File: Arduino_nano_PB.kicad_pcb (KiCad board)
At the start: 2 copper layers, 100 x 40 mm, 44 parts, among them CON1 BARREL_JACK, P1 CONN_01X02, P7 CONN_01X04, Q1 BC547, Q2 BC547, Q3 BC547, Q4 Q_NPN_EBC, Q5 Q_NPN_EBC, Q6 Q_NPN_EBC, Q7 Q_NPN_EBC, Q8 Q_NPN_EBC, U1 LM7805CT, U2 74HC595, U3 Matriz_5x7_Anodo_Filas, U4 Arduino_Nano

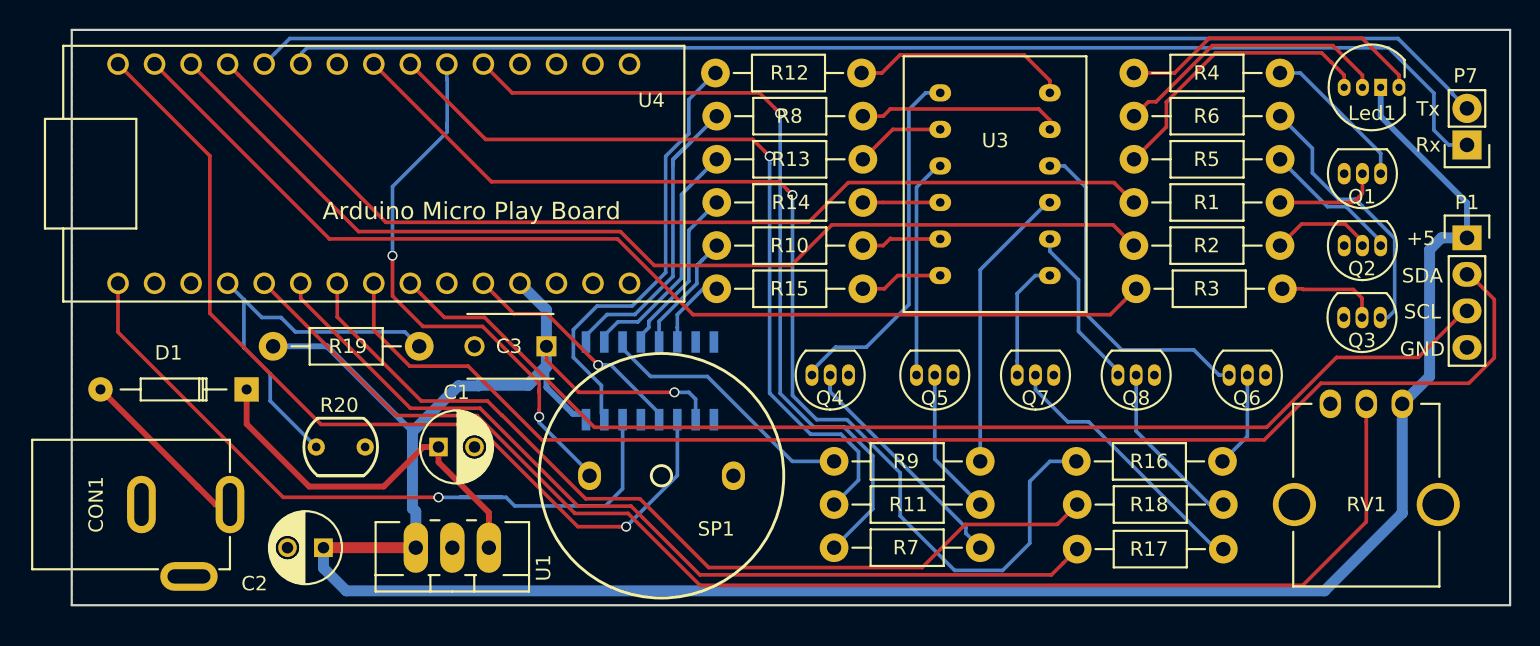
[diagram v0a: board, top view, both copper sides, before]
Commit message: añadir valores en esquema y reordenar PCB
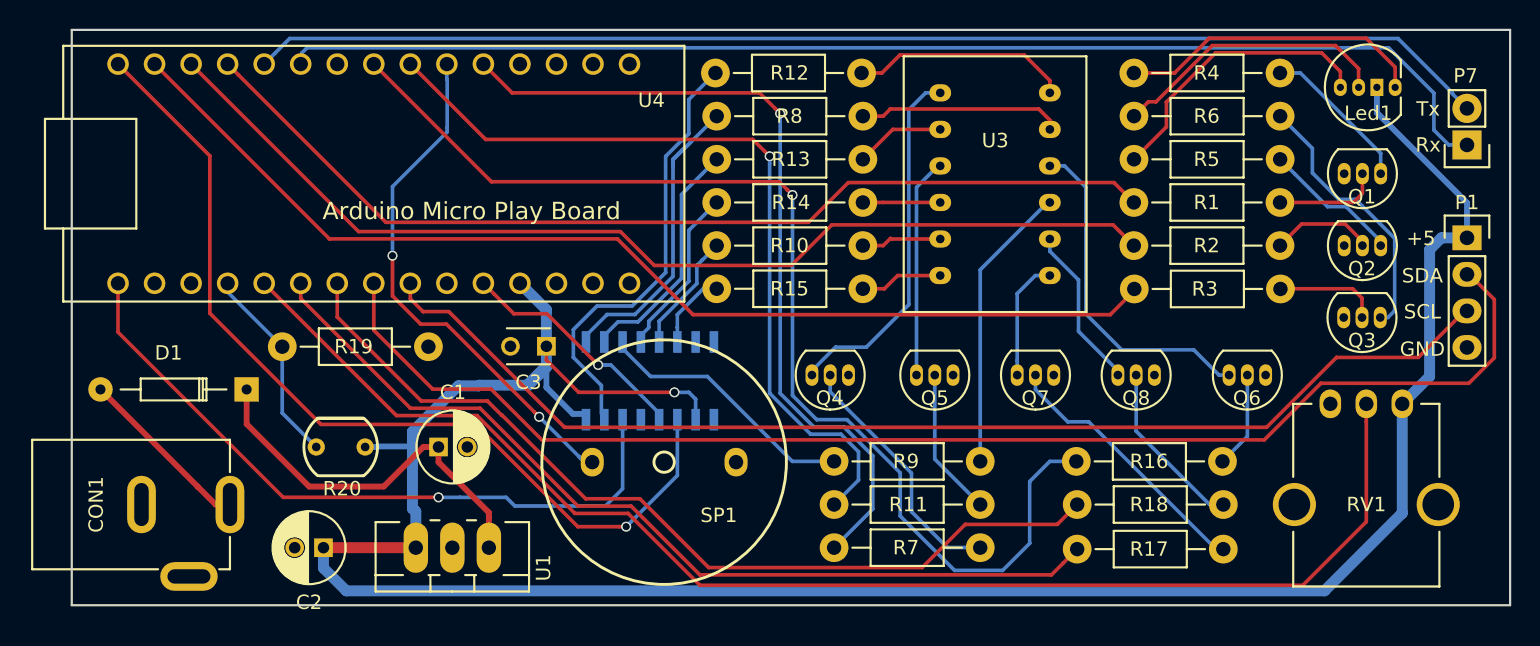
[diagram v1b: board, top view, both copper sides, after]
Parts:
- C1, C2: footprint Capacitors_ThroughHole:C_Radial_D5_L11_P2.5 -> Capacitors_ThroughHole:C_Radial_D5_L11_P2
- C3: value C -> 100n; footprint Capacitors_ThroughHole:C_Disc_D6_P5 -> Capacitors_ThroughHole:C_Disc_D3_P2.5
- D1: value D -> 1N4002
- Led1: value Led_RGB_Anodo_Comun -> Led_RGB
- Q4, Q5, Q6, Q7, Q8: value Q_NPN_EBC -> 2N3904BU
- R1, R2, R3: value R -> 4K7
- R10, R12, R13, R14, R15, R8, R9: value R -> 120
- R11, R16, R17, R18, R19, R7: value R -> 1K
- R20: value Photores -> LDR
- R4, R5, R6: value R -> 100
- RV1: value POT -> 10K
- SP1: value SPEAKER -> BUZZER
- U3: value Matriz_5x7_Anodo_Filas -> Matriz_5x7
- moved R19 10.8 mm to (134.8, 62.0), turned to 180 degrees
- moved SP1 0.96 mm to (151.2, 70.1)
- moved Led1 0.26 mm to (200.1, 44.0)
- moved R3 0.13 mm to (194.0, 58.0)
- turned R20 to 180 degrees
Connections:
- R19 pad 1: +5V -> GND
- R20 pad 1: /A0 -> +5V
- R20 pad 2: GND -> /A0
- U2 pad 7: (no net) -> Net-(U2-Pad7)
- U2 pad 9: (no net) -> Net-(U2-Pad9)
- U4 pad 1: (no net) -> Net-(U4-Pad1)
- U4 pad 17: (no net) -> +3V3
- U4 pad 18: (no net) -> Net-(U4-Pad18)
- U4 pad 2: (no net) -> Net-(U4-Pad2)
- U4 pad 25: (no net) -> Net-(U4-Pad25)
- U4 pad 28: (no net) -> Net-(U4-Pad28)
- U4 pad 3: (no net) -> Net-(U4-Pad3)
- U4 pad 30: (no net) -> Net-(U4-Pad30)
- U4 pad 9: (no net) -> Net-(U4-Pad9)
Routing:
- net /A0: track 27.6 -> 14.1 mm
- net +5V: track 190.5 -> 181.8 mm
- net /D13: track 51.7 -> 48.8 mm
- net /D3: track 38.8 -> 36.8 mm
- net Net-(Q4-Pad2): track 16.5 -> 17.7 mm
- net /A5: track 81.0 -> 81.6 mm

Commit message: Añadir serigrafia capa bottom
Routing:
- net Net-(C1-Pad1): track 27.1 -> 26.2 mm
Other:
- board text added: "Bu-D11"
- board text added: "Buzz-D3"
- board text added: "ClkIn-D12"
- board text added: "ClkOut-A7"
- board text added: "Col1-D2"
- board text added: "Col2-D4"
- board text added: "Col3-D5"
- board text added: "Col4-A2"
- board text added: "Col5-A3"
- board text added: "Din-D13"
- board text added: "Gn-D10"
- board text added: "LDR-A0"
- board text added: "Pot-A1"
- board text added: "Rd-D9"
- board text added: "Rx-D7"
- board text added: "SERIAL"
- board text added: "Tx-D8"
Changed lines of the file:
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@@
     (links 85)
     (no_connects 0)
-    (area 109.924999 39.924999 210.075001 80.075001)
+    (area 106.868999 39.924999 211.8998 80.075001)
     (thickness 1.6)
-    (drawings 11)
-    (tracks 399)
+    (drawings 28)
+    (tracks 398)
     (zones 0)
     (modules 44)
@@
     (47 F.CrtYd user)
     (48 B.Fab user)
-    (49 F.Fab user)
+    (49 F.Fab user hide)
   )
   (setup
@@
       (linewidth 0.100000)
       (plotframeref false)
-      (viasonmask true)
+      (viasonmask false)
       (mode 1)
       (useauxorigin false)
@@
   (module Sensores:LDR_TOKEN_PGM5_Series (layer F.Cu)
     (at 128.7 69 180)
-    (fp_text reference R20 (at -0.1 -2.9 180) (layer F.SilkS)
+    (fp_text reference R20 (at -0.0018 -2.9836 180) (layer F.SilkS)
       (effects (font (size 1 1) (thickness 0.15)))
     )
@@
     (descr "Radial Electrolytic Capacitor 5mm x Length 11mm, Pitch 2mm")
     (tags "Electrolytic Capacitor")
-    (fp_text reference C2 (at 1 -3.8 180) (layer F.SilkS)
+    (fp_text reference C2 (at 4.5386 -2.2574 180) (layer F.SilkS)
       (effects (font (size 1 1) (thickness 0.15)))
     )
@@
     )
   )
+  (gr_text ClkOut-A7 (at 156.0068 76.4794) (layer B.SilkS)
+    (effects (font (size 1 1) (thickness 0.2)) (justify mirror))
+  )
+  (gr_text ClkIn-D12 (at 156.0576 74.5998) (layer B.SilkS)
+    (effects (font (size 1 1) (thickness 0.2)) (justify mirror))
+  )
+  (gr_text Din-D13 (at 156.718 72.7964) (layer B.SilkS)
+    (effects (font (size 1 1) (thickness 0.2)) (justify mirror))
+  )
+  (gr_text Buzz-D3 (at 144.9324 72.9488) (layer B.SilkS)
+    (effects (font (size 1 1) (thickness 0.2)) (justify mirror))
+  )
+  (gr_text Bu-D11 (at 189.1284 48.9712) (layer B.SilkS)
+    (effects (font (size 1 1) (thickness 0.2)) (justify mirror))
+  )
+  (gr_text Gn-D10 (at 189.1538 45.974) (layer B.SilkS)
+    (effects (font (size 1 1) (thickness 0.2)) (justify mirror))
+  )
+  (gr_text Rd-D9 (at 189.1538 42.9768) (layer B.SilkS)
+    (effects (font (size 1 1) (thickness 0.2)) (justify mirror))
+  )
+  (gr_text LDR-A0 (at 128.8796 66.04) (layer B.SilkS)
+    (effects (font (size 1 1) (thickness 0.2)) (justify mirror))
+  )
+  (gr_text Pot-A1 (at 199.9996 69.9262) (layer B.SilkS)
+    (effects (font (size 1 1) (thickness 0.2)) (justify mirror))
+  )
+  (gr_text Col5-A3 (at 165.481 64.0334 90) (layer B.SilkS)
+    (effects (font (size 1 1) (thickness 0.2)) (justify mirror))
+  )
+  (gr_text Col4-A2 (at 172.7454 64.0334 90) (layer B.SilkS)
+    (effects (font (size 1 1) (thickness 0.2)) (justify mirror))
+  )
+  (gr_text Col3-D5 (at 179.7558 64.0334 90) (layer B.SilkS)
+    (effects (font (size 1 1) (thickness 0.2)) (justify mirror))
+  )
+  (gr_text Col2-D4 (at 186.7662 64.0334 90) (layer B.SilkS)
+    (effects (font (size 1 1) (thickness 0.2)) (justify mirror))
+  )
+  (gr_text Col1-D2 (at 194.4878 64.0334 90) (layer B.SilkS)
+    (effects (font (size 1 1) (thickness 0.2)) (justify mirror))
+  )
+  (gr_text Rx-D7 (at 203.1746 47.9552) (layer B.SilkS)
+    (effects (font (size 1 1) (thickness 0.2)) (justify mirror))
+  )
+  (gr_text Tx-D8 (at 203.1746 45.72) (layer B.SilkS)
+    (effects (font (size 1 1) (thickness 0.2)) (justify mirror))
+  )
+  (gr_text SERIAL (at 206.2734 42.799) (layer B.SilkS)
+    (effects (font (size 1 1) (thickness 0.2)) (justify mirror))
+  )
   (gr_text "Arduino Micro Play Board" (at 137.8 52.6) (layer F.SilkS)
     (effects (font (size 1.2 1.2) (thickness 0.2)))
@@
   (gr_line (start 110 40) (end 110 80) (layer Edge.Cuts) (width 0.15))
   (gr_line (start 110 40) (end 210 40) (layer Edge.Cuts) (width 0.15))
+  (segment (start 143 62) (end 143 63.462) (width 0.762) (layer B.Cu) (net 2))
+  (segment (start 143 63.462) (end 141.717223 64.744777) (width 0.762) (layer B.Cu) (net 2))
+  (segment (start 141.717223 64.744777) (end 138.305223 64.744777) (width 0.762) (layer B.Cu) (net 2))
+  (segment (start 138.305223 64.744777) (end 138.3 64.75) (width 0.762) (layer B.Cu) (net 2))
   (segment (start 200.7362 44) (end 200.7362 45.756611) (width 0.4064) (layer B.Cu) (net 2))
   (segment (start 200.7362 45.756611) (end 207 52.020411) (width 0.4064) (layer B.Cu) (net 2))
@@
   (segment (start 145.246 65.2) (end 151.9 65.2) (width 0.254) (layer F.Cu) (net 2))
   (via (at 151.9 65.2) (size 0.7) (drill 0.5) (layers F.Cu B.Cu) (net 2))
-  (segment (start 141.7556 64.7064) (end 138.3436 64.7064) (width 0.762) (layer B.Cu) (net 2))
-  (segment (start 138.3436 64.7064) (end 138.3 64.75) (width 0.762) (layer B.Cu) (net 2))
-  (segment (start 143 62) (end 143 63.462) (width 0.762) (layer B.Cu) (net 2) (status 10))
-  (segment (start 143 63.462) (end 141.7556 64.7064) (width 0.762) (layer B.Cu) (net 2))
   (segment (start 141.3564 64.75) (end 138.3 64.75) (width 0.4064) (layer B.Cu) (net 2))
   (segment (start 133.687638 67.939064) (end 136.876702 64.75) (width 0.762) (layer B.Cu) (net 2))
@@
   (segment (start 127 69) (end 124.6378 66.6378) (width 0.254) (layer B.Cu) (net 6))
   (segment (start 124.6378 66.6378) (end 124.6378 62.0268) (width 0.254) (layer B.Cu) (net 6))
-  (segment (start 135.5 69) (end 134.4436 69) (width 0.4064) (layer F.Cu) (net 7))
-  (segment (start 134.4436 69) (end 131.6936 71.75) (width 0.4064) (layer F.Cu) (net 7))
-  (segment (start 131.6936 71.75) (end 126.50922 71.75) (width 0.4064) (layer F.Cu) (net 7))
-  (segment (start 126.50922 71.75) (end 122.16 67.40078) (width 0.4064) (layer F.Cu) (net 7))
-  (segment (start 122.16 67.40078) (end 122.16 65) (width 0.4064) (layer F.Cu) (net 7))
-  (segment (start 135.5 69) (end 135.5 70.0564) (width 0.4064) (layer F.Cu) (net 7))
-  (segment (start 135.5 70.0564) (end 139 73.5564) (width 0.4064) (layer F.Cu) (net 7))
-  (segment (start 139 73.5564) (end 139 73.84354) (width 0.4064) (layer F.Cu) (net 7))
-  (segment (start 139 73.84354) (end 139 76) (width 0.4064) (layer F.Cu) (net 7) (status 20))
+  (segment (start 135.5 69) (end 135.5 70.412) (width 0.762) (layer F.Cu) (net 7))
+  (segment (start 139 73.912) (end 139 76) (width 0.762) (layer F.Cu) (net 7))
+  (segment (start 135.5 70.412) (end 139 73.912) (width 0.762) (layer F.Cu) (net 7))
+  (segment (start 122.16 65) (end 122.16 67.2198) (width 0.762) (layer F.Cu) (net 7))
+  (segment (start 122.16 67.2198) (end 125.6538 70.7136) (width 0.762) (layer F.Cu) (net 7))
+  (segment (start 125.6538 70.7136) (end 132.2832 70.7136) (width 0.762) (layer F.Cu) (net 7))
+  (segment (start 132.2832 70.7136) (end 133.9968 69) (width 0.762) (layer F.Cu) (net 7))
+  (segment (start 133.9968 69) (end 135.5 69) (width 0.762) (layer F.Cu) (net 7))
   (segment (start 159.251868 65.276109) (end 159.251868 46.313275) (width 0.254) (layer B.Cu) (net 8))
   (segment (start 163 76) (end 165.689574 73.310426) (width 0.254) (layer B.Cu) (net 8) (status 10))
@@
   (segment (start 123.38 57.62) (end 132.576022 66.816022) (width 0.254) (layer F.Cu) (net 40) (status 10))
   (segment (start 138.17915 66.816022) (end 144.97915 73.616022) (width 0.254) (layer F.Cu) (net 40))
-  (segment (start 121 73) (end 120 73) (width 0.4064) (layer F.Cu) (net 41) (status 30))
-  (segment (start 118.75 71.75) (end 112 65) (width 0.4064) (layer F.Cu) (net 41) (status 20))
-  (segment (start 120 73) (end 118.75 71.75) (width 0.4064) (layer F.Cu) (net 41) (status 10))
+  (segment (start 121 73) (end 120 73) (width 0.762) (layer F.Cu) (net 41) (status 30))
+  (segment (start 118.75 71.75) (end 112 65) (width 0.762) (layer F.Cu) (net 41) (status 20))
+  (segment (start 120 73) (end 118.75 71.75) (width 0.762) (layer F.Cu) (net 41) (status 10))
   (segment (start 142.497241 66.902759) (end 145.266682 69.6722) (width 0.254) (layer B.Cu) (net 42))
   (segment (start 145.266682 69.6722) (end 145.5496 69.955118) (width 0.254) (layer B.Cu) (net 42))

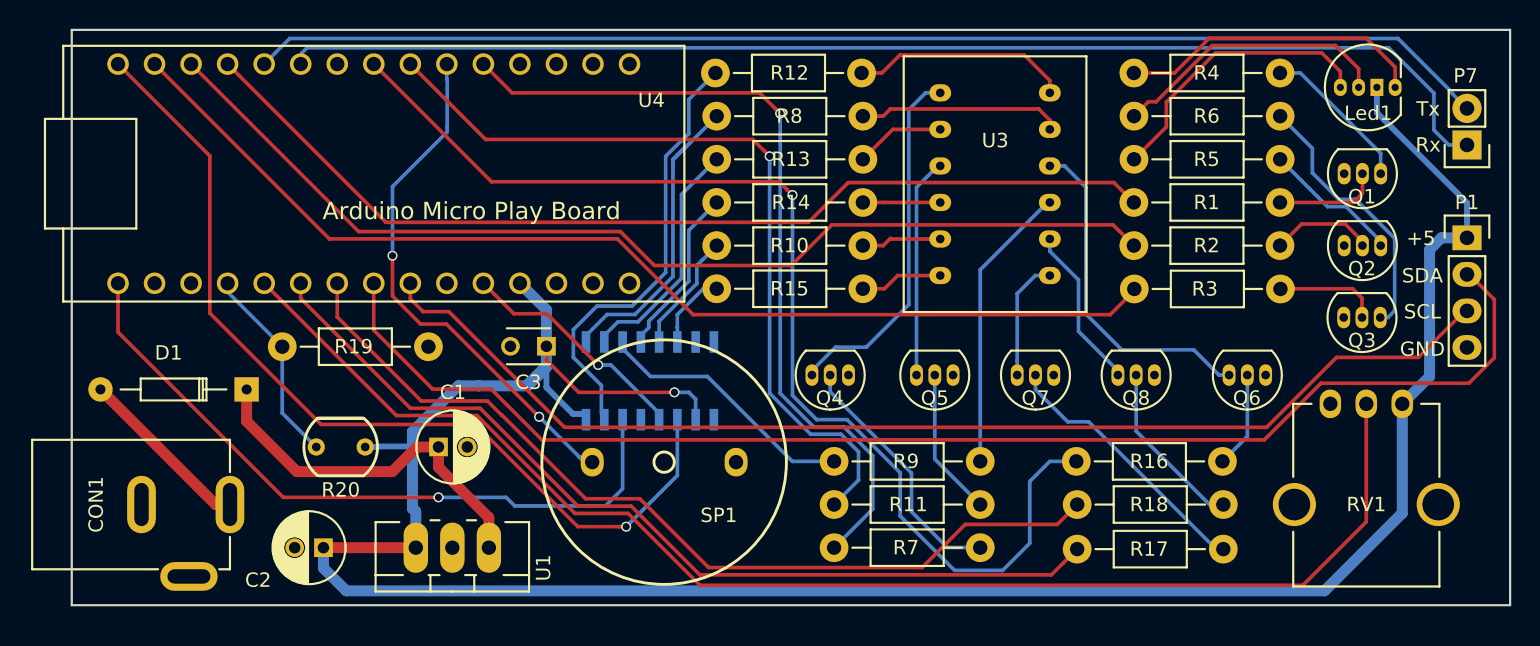
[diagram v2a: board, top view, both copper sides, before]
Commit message: corregir errata en readme y capa de serigrafia superior
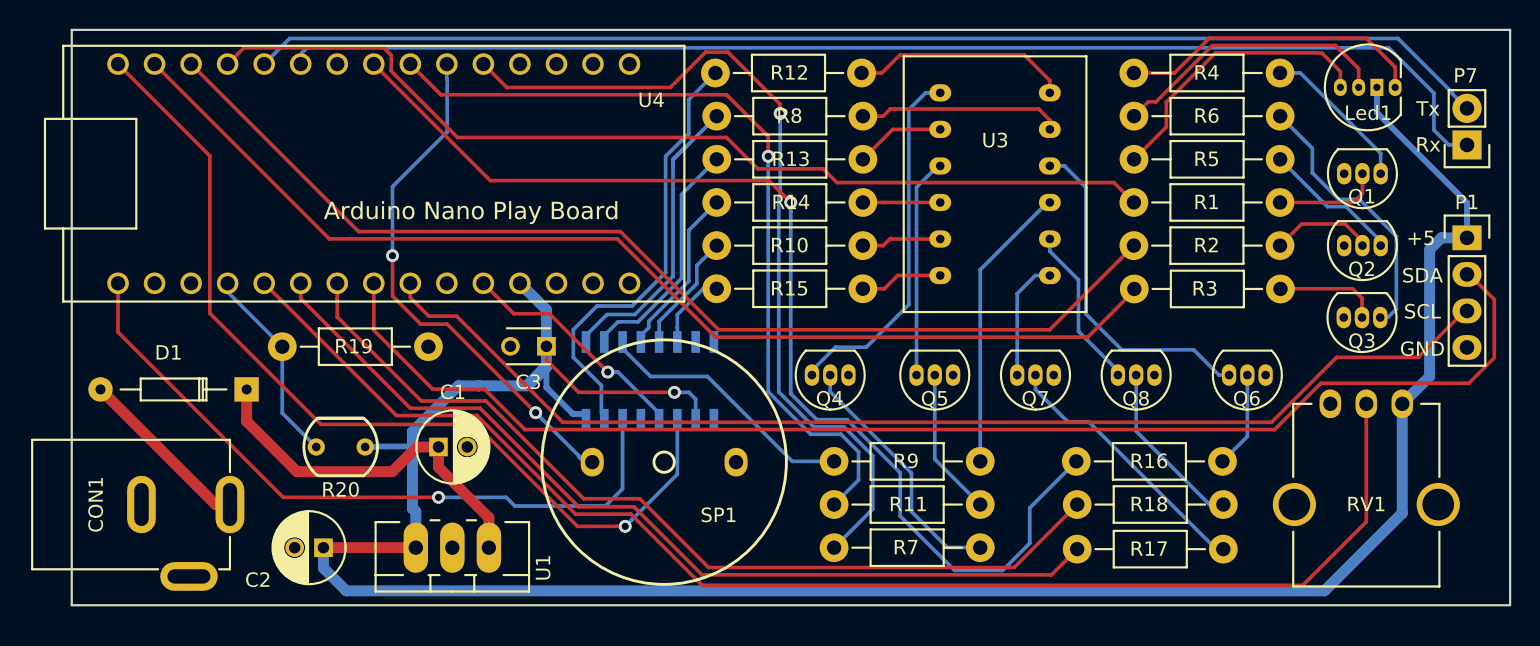
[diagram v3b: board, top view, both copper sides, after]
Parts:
- Q1, Q2, Q3, Q4, Q5, Q6, Q7, Q8: footprint TO_SOT_Packages_THT:TO-92_Inline_Narrow_Oval -> Transistors:TO-92_EnLinea_Estrecho_Oval
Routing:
- net /D10: track 73.1 -> 75.6 mm
- net /D2: track 57.3 -> 59.7 mm
- net /D5: track 79.0 -> 77.5 mm
- net /D11: track 76.2 -> 77.5 mm
- net /D4: track 56.3 -> 57.1 mm
- net /D9: track 69.3 -> 68.6 mm
- net /A4: track 93.4 -> 92.8 mm
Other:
- net class Default: via_dia 0.7 -> 0.9
- rule pad_to_mask_clearance: 0.1016 -> 0.1778
- board text added: "Arduino Nano Play Board"
- board text removed: "Arduino Micro Play Board"

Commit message: modificar tamaños de taladros en led RGB y resistencias
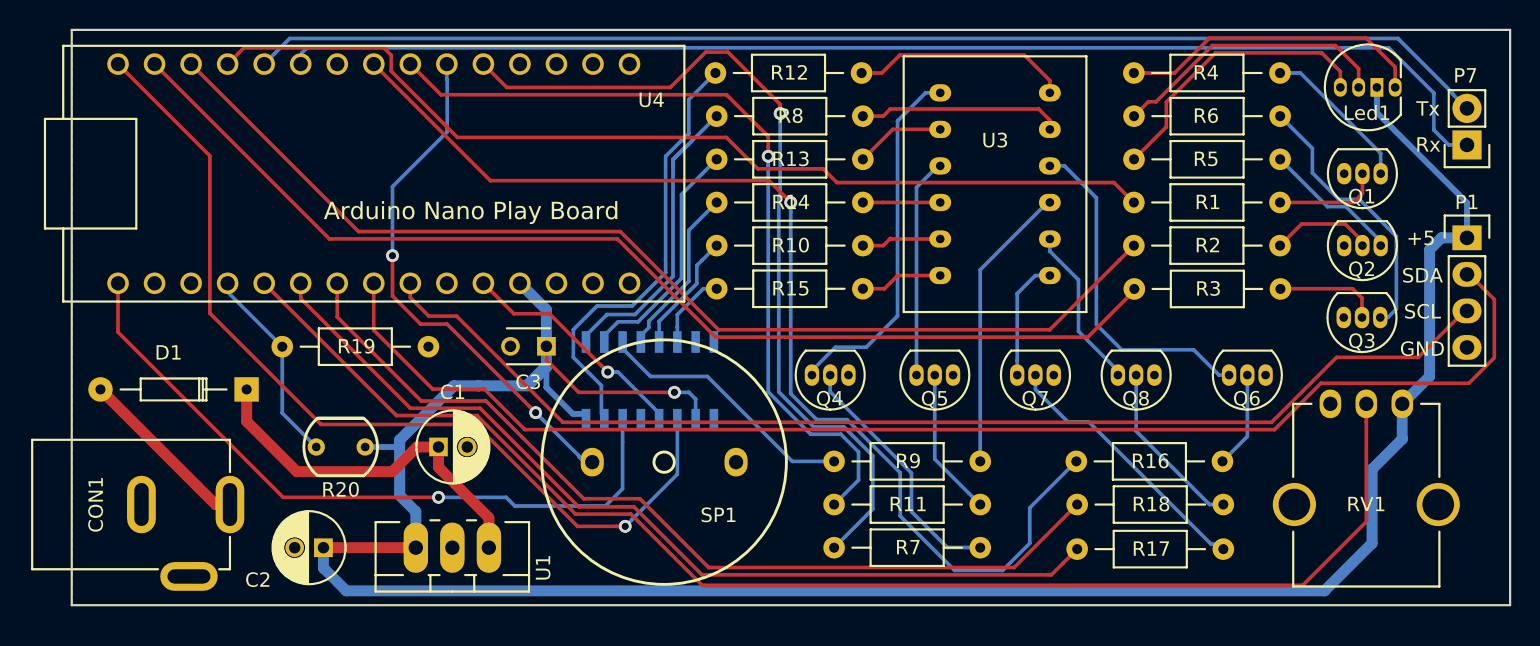
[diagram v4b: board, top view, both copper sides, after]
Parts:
- R1, R10, R11, R12, R13, R14, R15, R16, R17, R18, R19, R2, R3, R4, R5, R6, R7, R8, R9: footprint Resistors_ThroughHole:Resistor_Horizontal_RM10mm -> Resistencias:Resistencia_1_4_W_10_mm
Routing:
- net +5V: track 181.8 -> 176.5 mm
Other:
- board text added: "I2C"

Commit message: corrige issue #2
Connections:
- U2 pad 12: /A7 -> /D6
- U4 pad 26: /A7 -> Net-(U4-Pad26)
- U4 pad 9: Net-(U4-Pad9) -> /D6
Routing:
- net /D6: track 0.00 -> 38.1 mm, vias 0 -> 3
- net /A7: track 16.4 -> 0.00 mm, vias 1 -> 0
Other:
- board text added: "ClkOut-D6"
- board text removed: "ClkOut-A7"
